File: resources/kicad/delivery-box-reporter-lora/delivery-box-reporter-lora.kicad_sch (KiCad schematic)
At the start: 16 parts, among them J1 Power 4v-6v, J2 Power 4v-6v, Q2 2N3904, U1 ESP8266 D1 Mini, U2 TP4056_Battery_Charger_Board, U4 TLV803EB33VDBZR, U5 MCP1702-3302E

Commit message: Mostly changes to the box and board design
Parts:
- J1: value Power 4v-6v -> Solar Power 4v-6v
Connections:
- net +3.3V: now also U6.5 (3.3v); no longer U6.1 (3.3v)
- net Earth: now also U6.1 (GND); no longer U6.5 (GND)
- net SS RX: now also U6.2 (TX); no longer U6.4 (TX)
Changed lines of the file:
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@@
 			)
 		)
-		(property "Value" "Power 4v-6v"
+		(property "Value" "Solar Power 4v-6v"
 			(at 45.212 96.012 0)
 			(effects

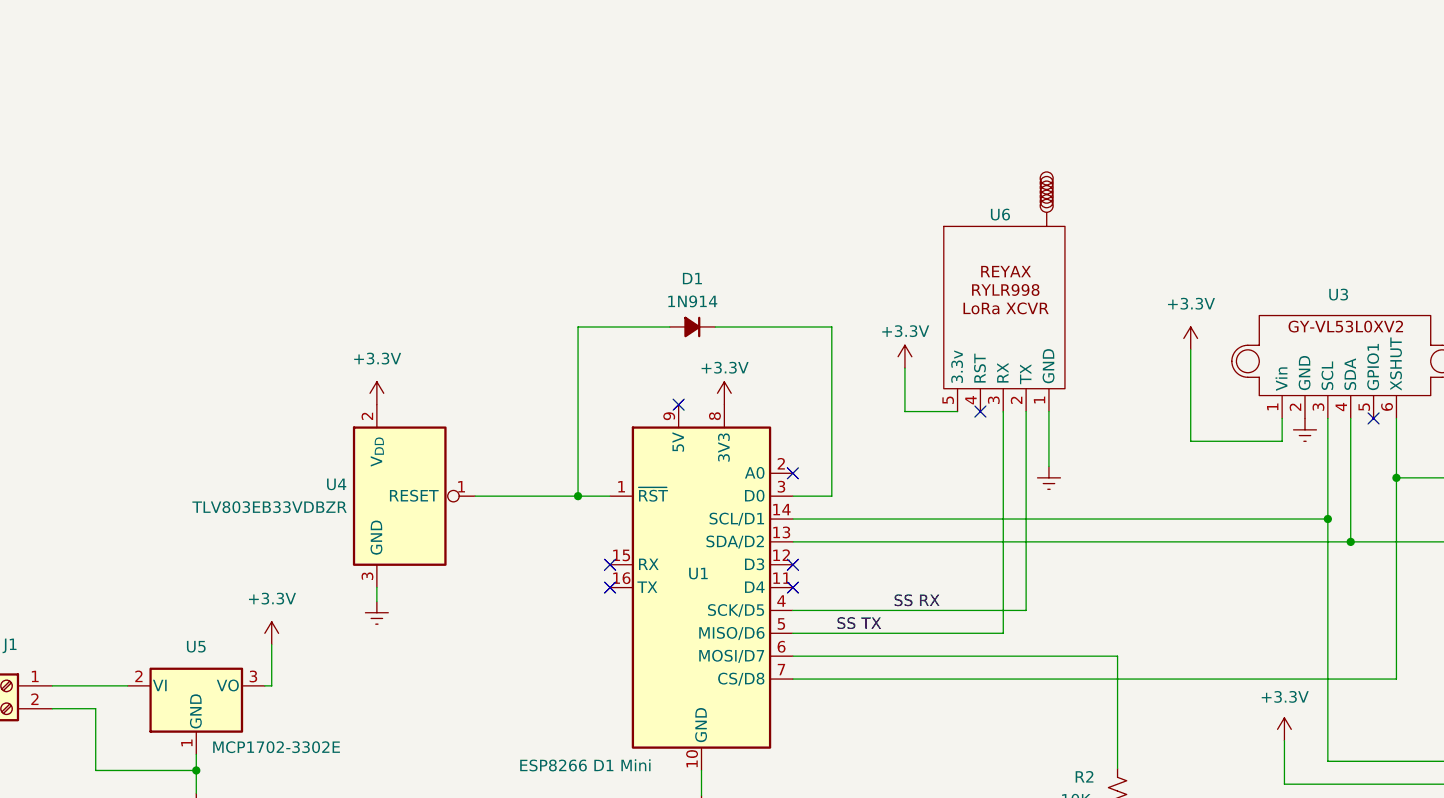
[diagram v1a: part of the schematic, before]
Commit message: Changes to the enclosures, presentation, and code
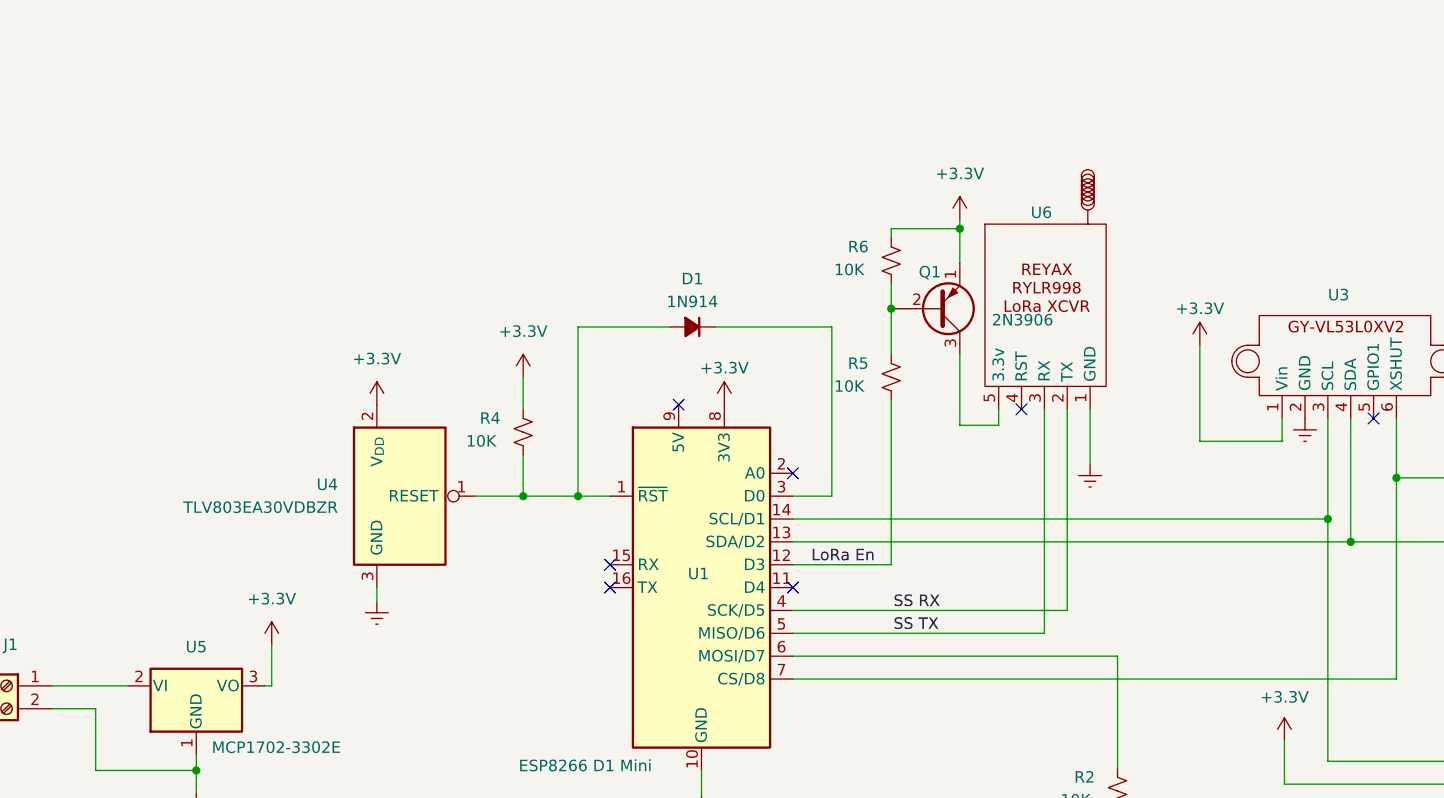
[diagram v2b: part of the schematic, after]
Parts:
- added Q1: 2N3906, Davids_Footprints:MMBT3904-7-F_SOT-23-3, symbol Transistor_BJT:2N3906
- added R4, R5, R6: 10K, Resistor_SMD:R_0805_2012Metric, symbol Device:R_Small_US
- U4: value TLV803EB33VDBZR -> TLV803EA30VDBZR
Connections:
- net +3.3V: now also Q1.1 (E), R4.2, R6.2; no longer U6.5 (3.3v)
- net at D1.2 (A), U1.1 (~{RST}), U4.1 (RESET): now also R4.1
- net LoRa En: now reaches U1.12 (D3)
- net LoRa En: now also R5.1
- new net: Q1.3 (C), U6.5 (3.3v)
- new net: Q1.2 (B), R5.2, R6.1
- no-connect marks 8 -> 7
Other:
- moved on the sheet: U6

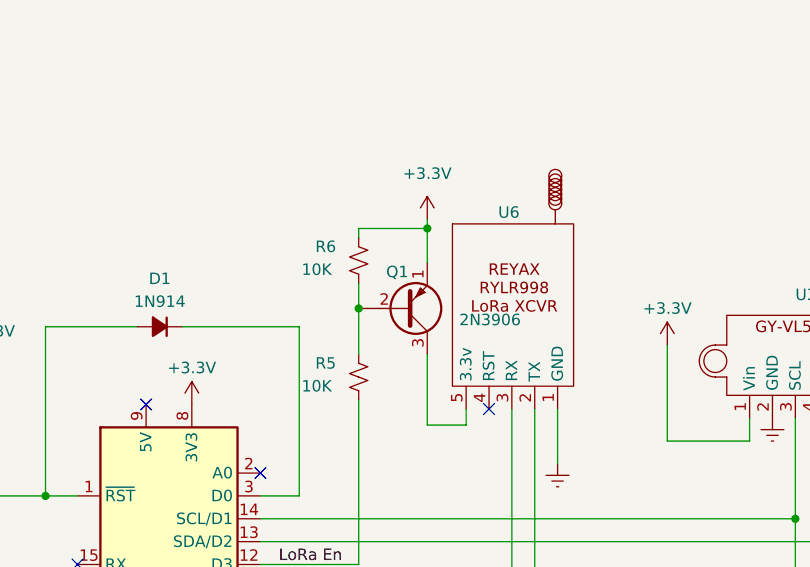
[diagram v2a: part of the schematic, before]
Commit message: Pulled code to enable and disable LORA radio into a separate function
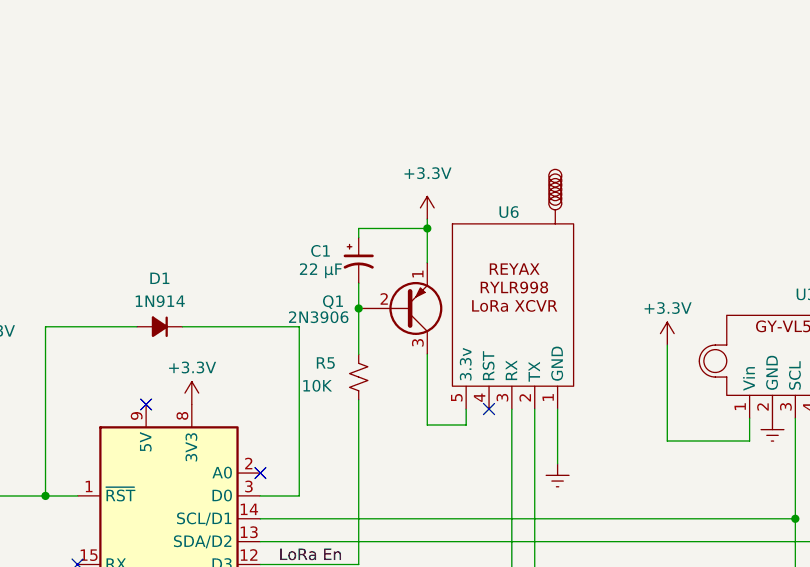
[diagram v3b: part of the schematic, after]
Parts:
- C1: renamed from R6; value 10K -> 22 μF; symbol Device:R_Small_US -> Device:C_Polarized_Small_US
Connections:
- net +3.3V: now also C1.1; no longer C1.2
- net at Q1.2 (B), R5.2: now also C1.2; no longer C1.1
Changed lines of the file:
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@@
 	)
 	(symbol
-		(lib_id "Device:R_Small_US")
-		(at 146.558 47.498 180)
-		(unit 1)
-		(exclude_from_sim no)
-		(in_bom yes)
-		(on_board yes)
-		(dnp no)
-		(property "Reference" "R6"
-			(at 141.732 45.974 0)
+		(lib_id "Device:C_Polarized_Small_US")
+		(at 146.558 47.498 0)
+		(unit 1)
+		(exclude_from_sim no)
+		(in_bom yes)
+		(on_board yes)
+		(dnp no)
+		(property "Reference" "C1"
+			(at 143.51 46.482 0)
 			(effects
 				(font
@@
 			)
 		)
-		(property "Value" "10K"
-			(at 140.208 48.514 0)
+		(property "Value" "22 μF"
+			(at 144.78 48.514 0)
 			(effects
 				(font
@@
 			)
 		)
-		(property "Description" "Resistor, small US symbol"
+		(property "Description" "Polarized capacitor, small US symbol"
 			(at 146.558 47.498 0)
 			(effects
@@
 			(project "delivery-box-reporter-lora"
 				(path "/b5a49f66-f3e1-4174-95b7-6fa32f14e918"
-					(reference "R6")
+					(reference "C1")
 					(unit 1)
 				)
@@
 		(dnp no)
 		(property "Reference" "Q1"
-			(at 149.606 48.768 0)
+			(at 142.494 52.07 0)
 			(effects
 				(font
@@
 		)
 		(property "Value" "2N3906"
-			(at 157.734 54.1019 0)
-			(effects
-				(font
+			(at 138.684 53.848 0)
+			(effects
+				(font

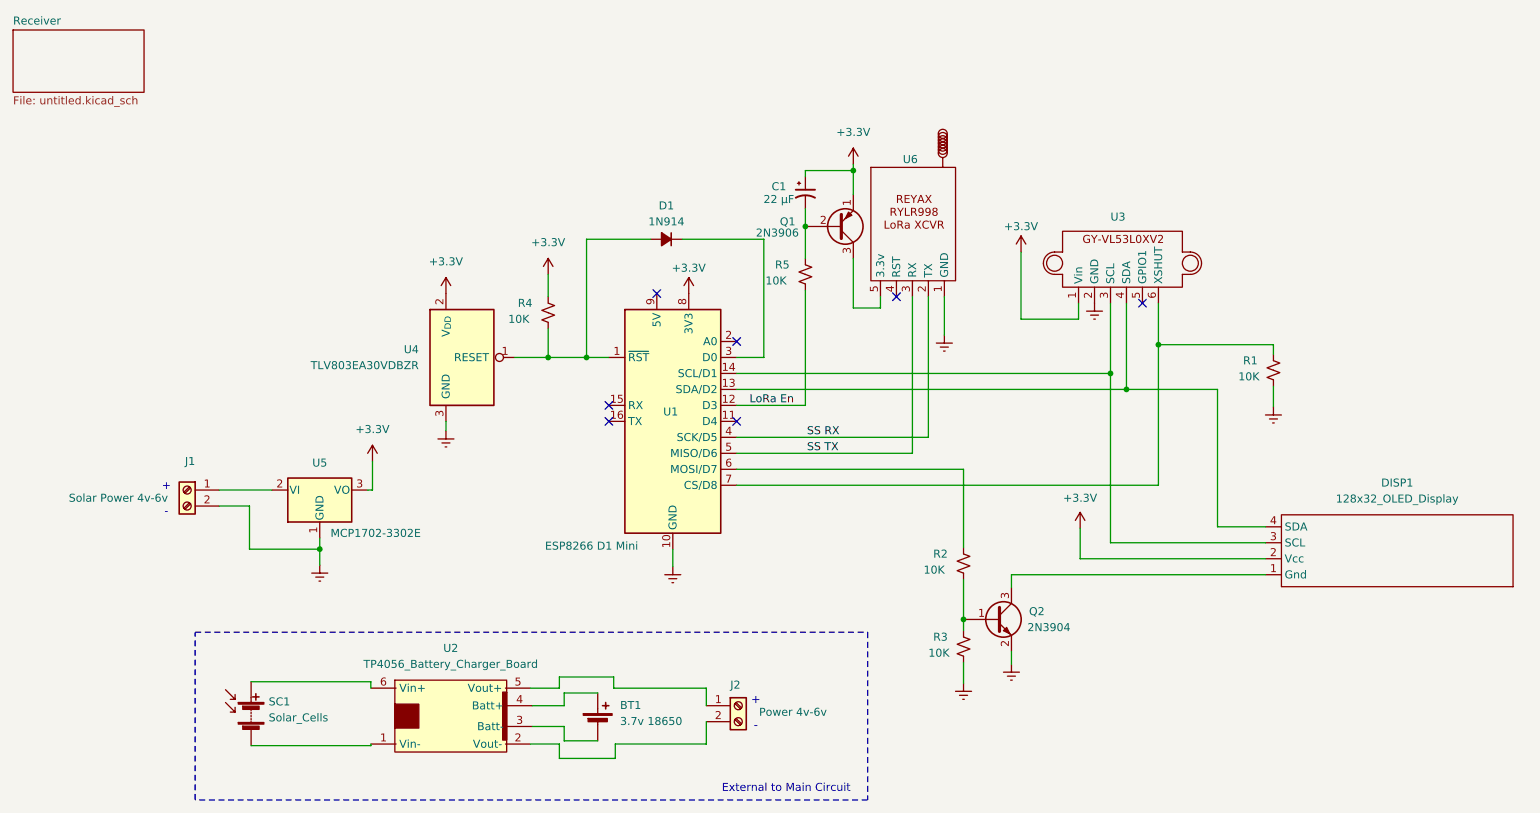
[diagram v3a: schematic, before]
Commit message: Small changes to the LoRa power circuit.
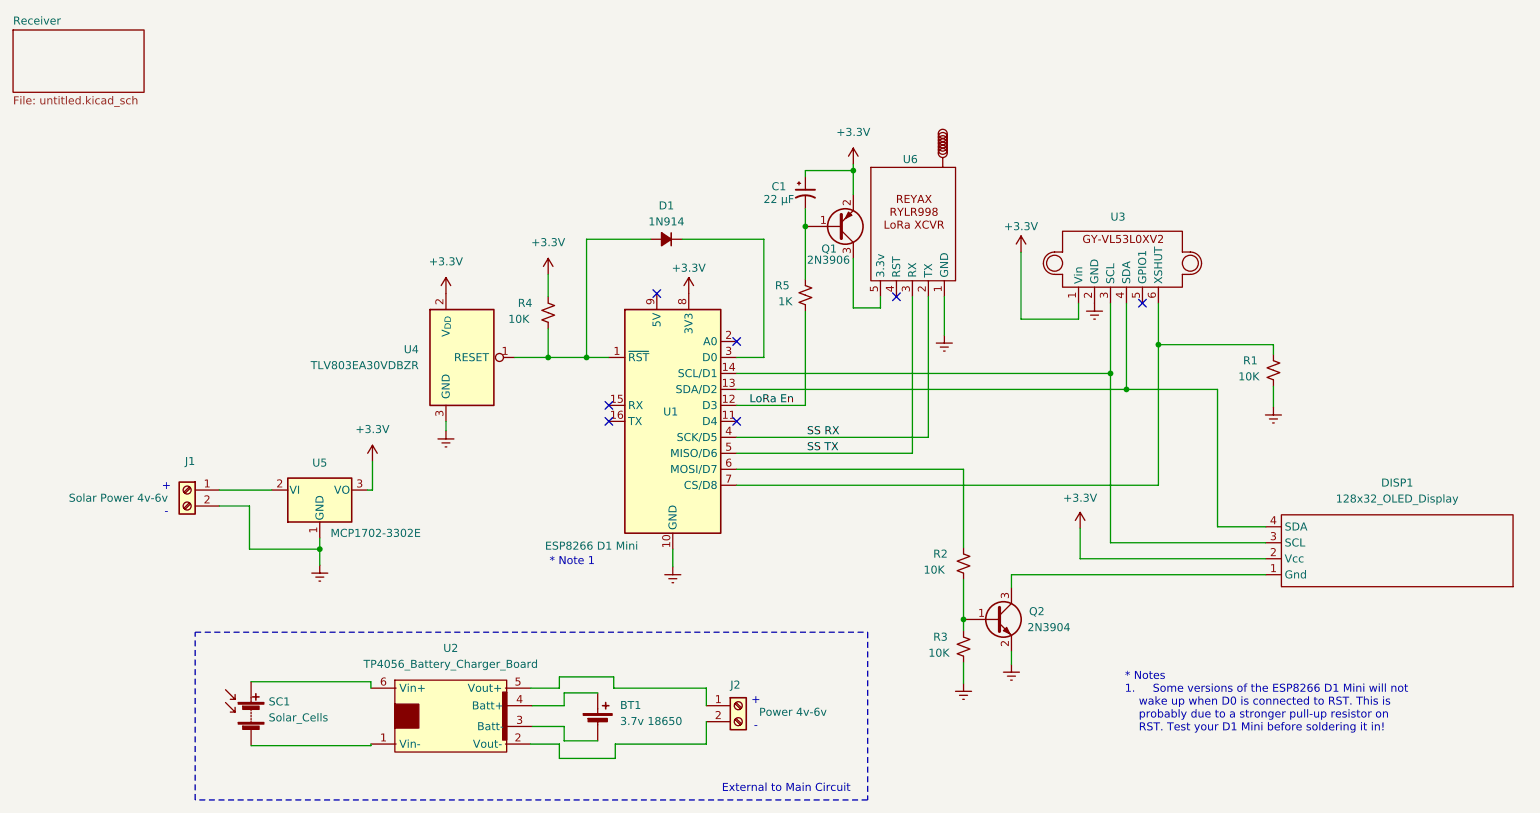
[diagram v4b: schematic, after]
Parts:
- R5: value 10K -> 1K
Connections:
- net +3.3V: now also Q1.2 (E); no longer Q1.1 (E)
- net at C1.2, R5.2: now also Q1.1 (B); no longer Q1.2 (B)
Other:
- note added: "* Note 1"
- note added: "* Notes 1. Some versions of the ESP8266 D1 Mini will not wake up when D0 is connected to RST. This is probably due to a stronger pull-up resistor on RST. Test your D1 Mini before soldering it in!"
- title: Delivery Box Reporter Transmitter -> Delivery Box Reporter Transmitter LoRa
- moved on the sheet: R5
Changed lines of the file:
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@@
 	(paper "A")
 	(title_block
-		(title "Delivery Box Reporter Transmitter")
-		(date "2025-02-08")
-		(rev "2.2.0")
+		(title "Delivery Box Reporter Transmitter LoRa")
+		(date "2025-03-04")
+		(rev "2.2.1")
 	)
 	(junction
@@
 	)
 	(junction
+		(at 111.76 73.66)
+		(diameter 0)
+		(color 0 0 0 0)
+	)
+	(junction
 		(at 202.692 71.628)
 		(diameter 0)
@@
 	)
 	(junction
-		(at 111.76 73.66)
-		(diameter 0)
-		(color 0 0 0 0)
-	)
-	(junction
 		(at 146.558 52.832)
 		(diameter 0)
@@
 	(wire
 		(pts
+			(xy 111.76 73.66) (xy 115.316 73.66)
+		)
+		(stroke
+			(width 0)
+			(type default)
+		)
+	)
+	(wire
+		(pts
 			(xy 69.342 104.14) (xy 69.342 106.68)
 		)
@@
 	(wire
 		(pts
+			(xy 105.664 73.66) (xy 111.76 73.66)
+		)
+		(stroke
+			(width 0)
+			(type default)
+		)
+	)
+	(wire
+		(pts
 			(xy 158.496 64.008) (xy 158.496 65.786)
 		)
@@
 	(wire
 		(pts
-			(xy 111.76 73.66) (xy 115.316 73.66)
-		)
-		(stroke
-			(width 0)
-			(type default)
-		)
-	)
-	(wire
-		(pts
 			(xy 107.442 126.238) (xy 107.442 124.46)
 		)
@@
 	(wire
 		(pts
-			(xy 105.664 73.66) (xy 111.76 73.66)
+			(xy 111.76 54.864) (xy 111.76 73.66)
 		)
 		(stroke
@@
 	(wire
 		(pts
-			(xy 111.76 54.864) (xy 111.76 73.66)
-		)
-		(stroke
-			(width 0)
-			(type default)
-		)
-	)
-	(wire
-		(pts
 			(xy 195.072 76.2) (xy 195.072 103.124)
 		)
@@
 	(wire
 		(pts
-			(xy 146.558 52.832) (xy 146.558 57.912)
-		)
-		(stroke
-			(width 0)
-			(type default)
-		)
-	)
-	(wire
-		(pts
-			(xy 146.558 62.992) (xy 146.558 81.28)
+			(xy 146.558 52.832) (xy 146.558 61.214)
+		)
+		(stroke
+			(width 0)
+			(type default)
+		)
+	)
+	(wire
+		(pts
+			(xy 146.558 66.294) (xy 146.558 81.28)
 		)
 		(stroke
@@
 		)
 	)
+	(text "* Notes\n1. 	Some versions of the ESP8266 D1 Mini will not\n	wake up when D0 is connected to RST. This is\n	probably due to a stronger pull-up resistor on\n	RST. Test your D1 Mini before soldering it in!"
+		(exclude_from_sim no)
+		(at 197.358 128.524 0)
+		(effects
+			(font
+				(size 1.27 1.27)
+			)
+			(justify left)
+		)
+	)
 	(text "-"
 		(exclude_from_sim no)
@@
 		(exclude_from_sim no)
 		(at 44.958 98.298 0)
+		(effects
+			(font
+				(size 1.27 1.27)
+			)
+		)
+	)
+	(text "* Note 1"
+		(exclude_from_sim no)
+		(at 109.474 106.172 0)
 		(effects
 			(font
@@
 	(symbol
 		(lib_id "Device:R_Small_US")
-		(at 146.558 60.452 180)
+		(at 146.558 63.754 180)
 		(unit 1)
 		(exclude_from_sim no)
@@
 		(dnp no)
 		(property "Reference" "R5"
-			(at 141.732 58.928 0)
+			(at 141.732 62.23 0)
 			(effects
 				(font
@@
 			)
 		)
-		(property "Value" "10K"
-			(at 140.208 61.468 0)
+		(property "Value" "1K"
+			(at 142.24 64.77 0)
 			(effects
 				(font
@@
 		)
 		(property "Footprint" "Resistor_SMD:R_0805_2012Metric"
-			(at 146.558 60.452 0)
+			(at 146.558 63.754 0)
 			(effects
 				(font
@@
 		)
 		(property "Datasheet" "~"
-			(at 146.558 60.452 0)
+			(at 146.558 63.754 0)
 			(effects
 				(font
@@
 		)
 		(property "Description" "Resistor, small US symbol"
-			(at 146.558 60.452 0)
+			(at 146.558 63.754 0)
 			(effects
 				(font
@@
 		(dnp no)
 		(property "Reference" "Q1"
-			(at 142.494 52.07 0)
+			(at 149.098 56.388 0)
 			(effects
 				(font
@@
 		)
 		(property "Value" "2N3906"
-			(at 138.684 53.848 0)
-			(effects
-				(font
+			(at 146.812 58.166 0)
+			(effects
+				(font
